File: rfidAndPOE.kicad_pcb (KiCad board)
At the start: 4 copper layers, 100 x 50 mm, 126 parts, among them J1 0813-1X1T-57-F, J2 SWD, J3 MCU Port B, J4 MCU Port C, P1 PoE-, P2 PoE+, P3 GND, P4 +5V, P5 +12V, P6 +3V3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

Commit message: Placed and routed all isolated PoE components.
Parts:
- moved R9 146.9 mm to (123.1, 47.5)
- moved R1 141.5 mm to (120.1, 43.9)
- moved R8 141.1 mm to (120.1, 42.1)
- moved D4 122.6 mm to (127.4, 44.6), turned to 90 degrees
- moved D7 121.4 mm to (123.2, 45.7)
- moved Q3 8.56 mm to (123.5, 43.0), turned to 270 degrees
- moved D3 6.78 mm to (122.4, 39.5), turned to 90 degrees
- moved R6 6.50 mm to (124.3, 39.6), turned to 90 degrees
- moved U5 3.60 mm to (129.9, 61.5)
- moved U3 2.53 mm to (133.8, 46.9)
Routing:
- net /PVcc: track 14.7 -> 42.1 mm, vias 2 -> 3
- net Net-(R1-Pad1): track 0.00 -> 25.1 mm, vias 0 -> 2
- net Net-(D7-Pad1): track 0.00 -> 24.3 mm, vias 0 -> 3
- net GNDA: track 41.8 -> 61.2 mm, vias 8 -> 19
- net Net-(D7-Pad2): track 0.00 -> 8.62 mm
- net Net-(D4-Pad2): track 0.00 -> 6.55 mm
- net Net-(R6-Pad2): track 0.00 -> 2.70 mm
- net Net-(D3-Pad1): track 0.00 -> 2.04 mm
- added copper zone on B.Cu, net GNDA
- added copper zone on F.Cu, net GNDA

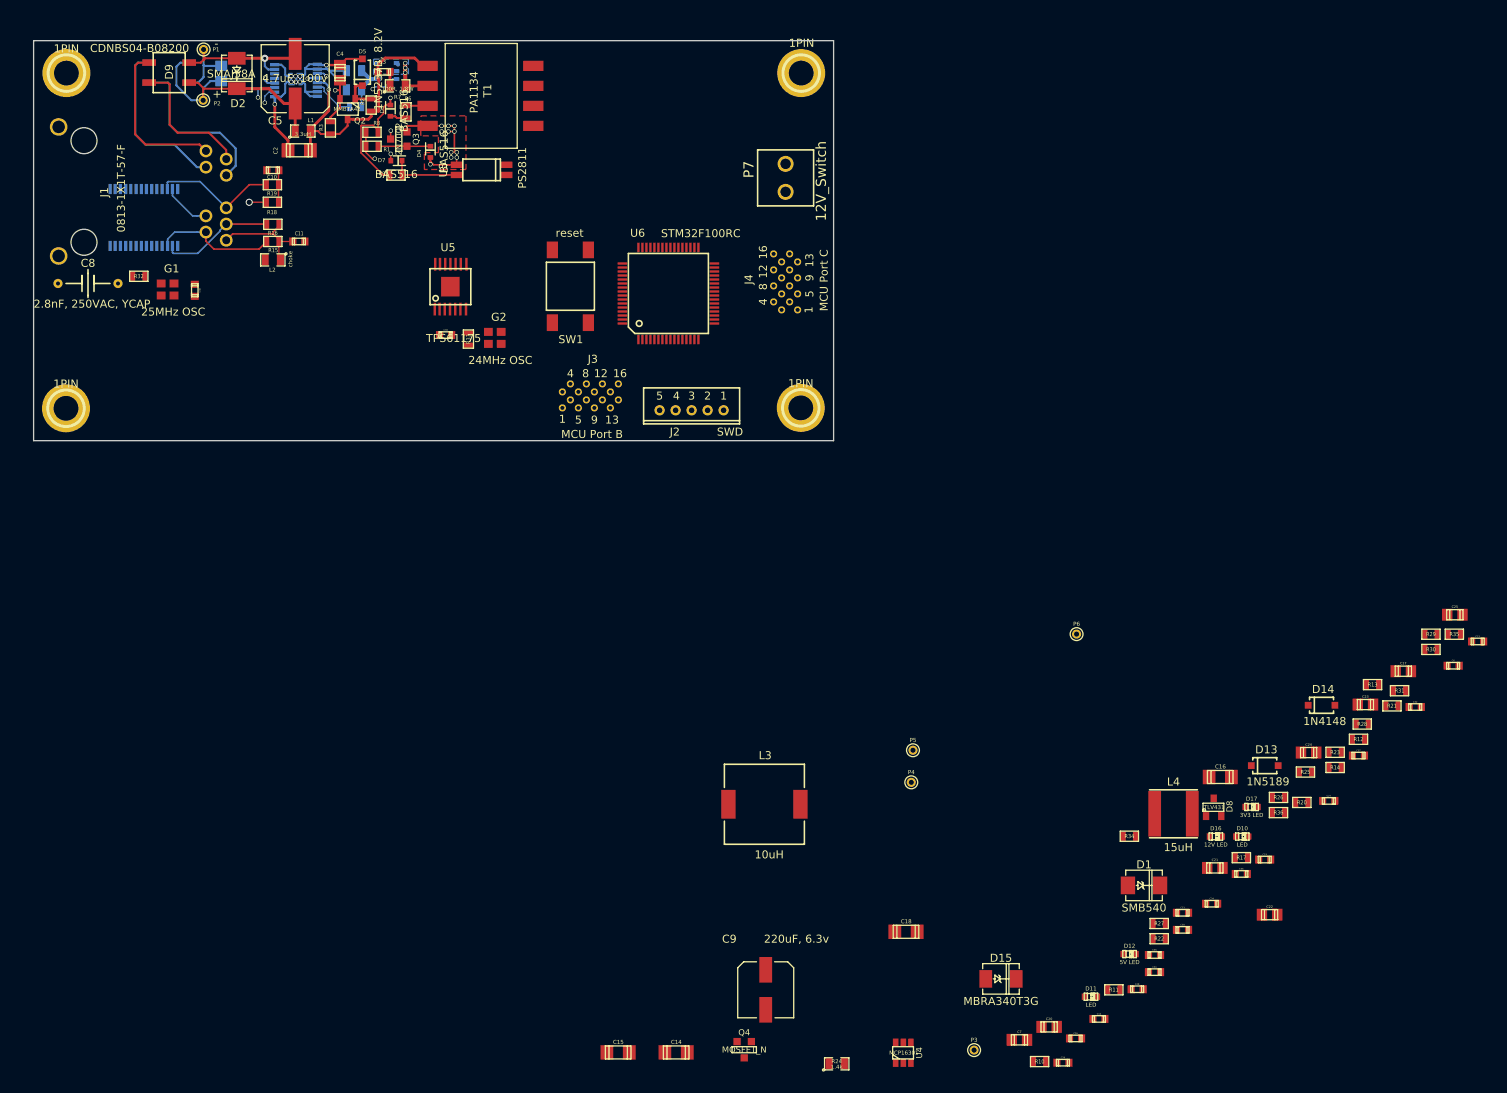
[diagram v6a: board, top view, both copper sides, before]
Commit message: Organized parts in to general sections (rest of PoE stuff, microcontroller, ethernet phy, 5v supply, and 3.3v supply are the groupings).
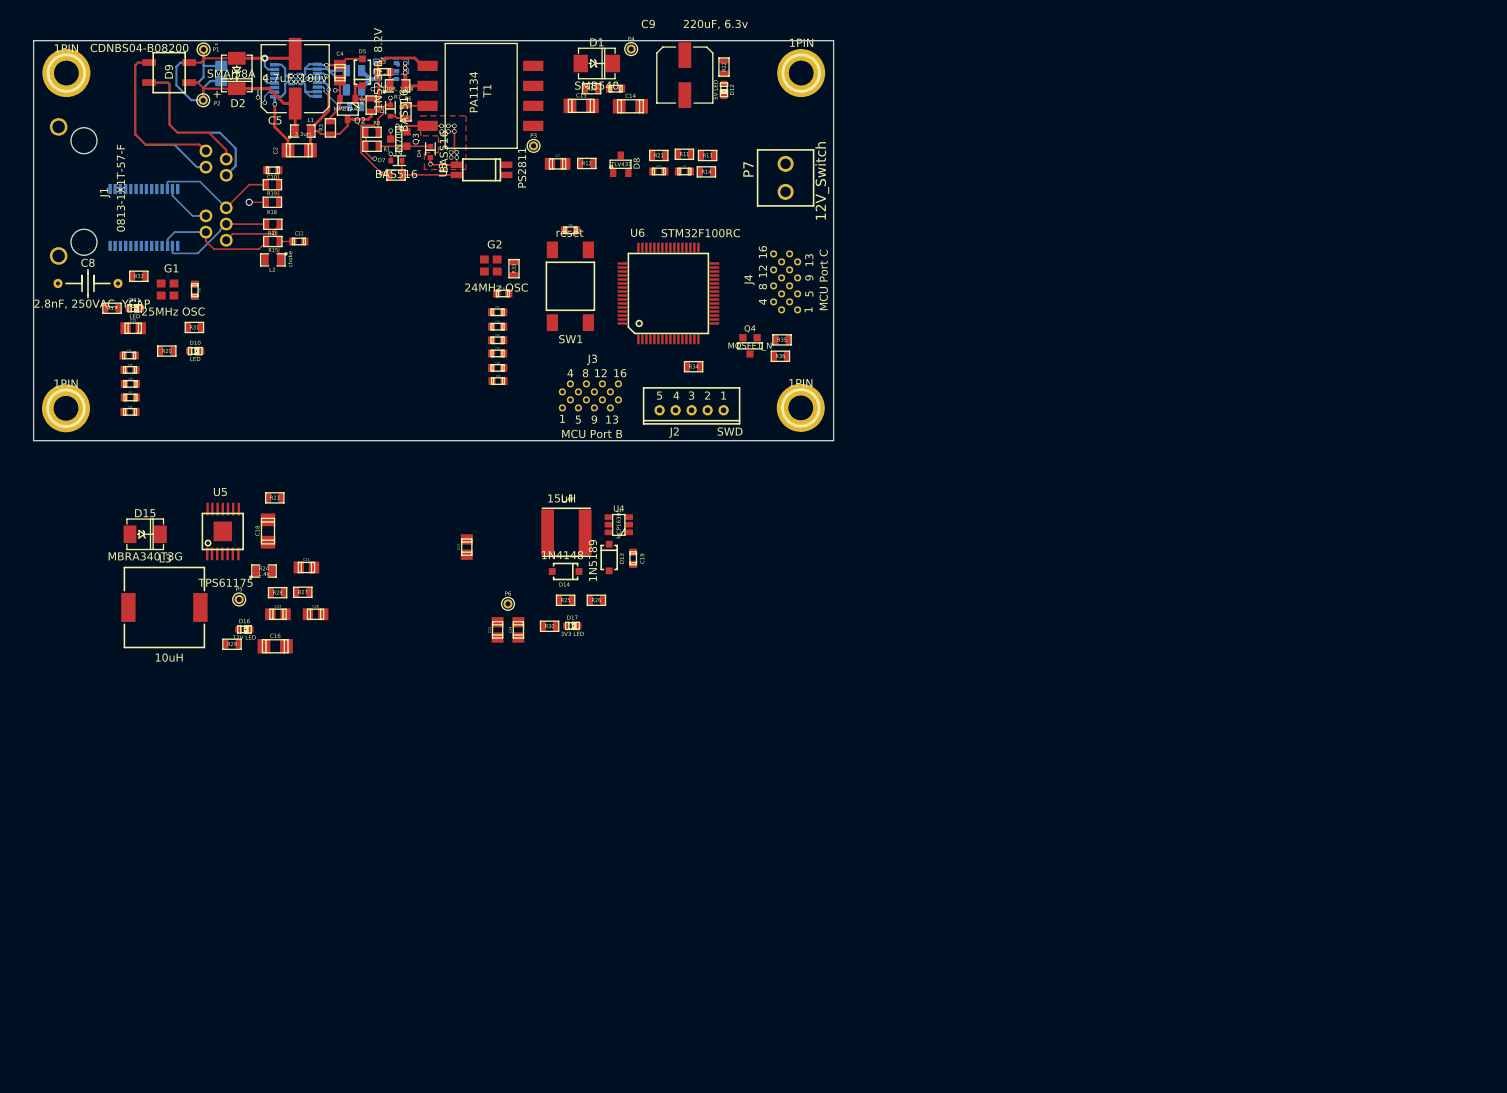
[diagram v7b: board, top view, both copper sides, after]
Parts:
- moved C25 169.0 mm to (90.2, 66.7)
- moved C27 158.1 mm to (89.9, 75.3)
- moved R31 157.3 mm to (97.9, 66.5)
- moved R17 157.0 mm to (87.6, 64.2)
- moved R20 152.7 mm to (94.5, 69.5)
- moved R29 149.9 mm to (102.6, 106.2)
- moved C31 149.6 mm to (89.8, 70.0)
- moved D11 147.3 mm to (90.5, 64.2)
- moved C28 146.8 mm to (89.9, 73.6)
- moved C29 145.3 mm to (89.8, 71.8)
- moved D10 144.3 mm to (98.0, 69.5)
- moved C26 141.8 mm to (89.8, 77.1)
- moved R28 136.6 mm to (108.3, 99.7)
- moved C23 136.4 mm to (108.3, 102.4)
- moved R23 136.3 mm to (108.0, 87.8)
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
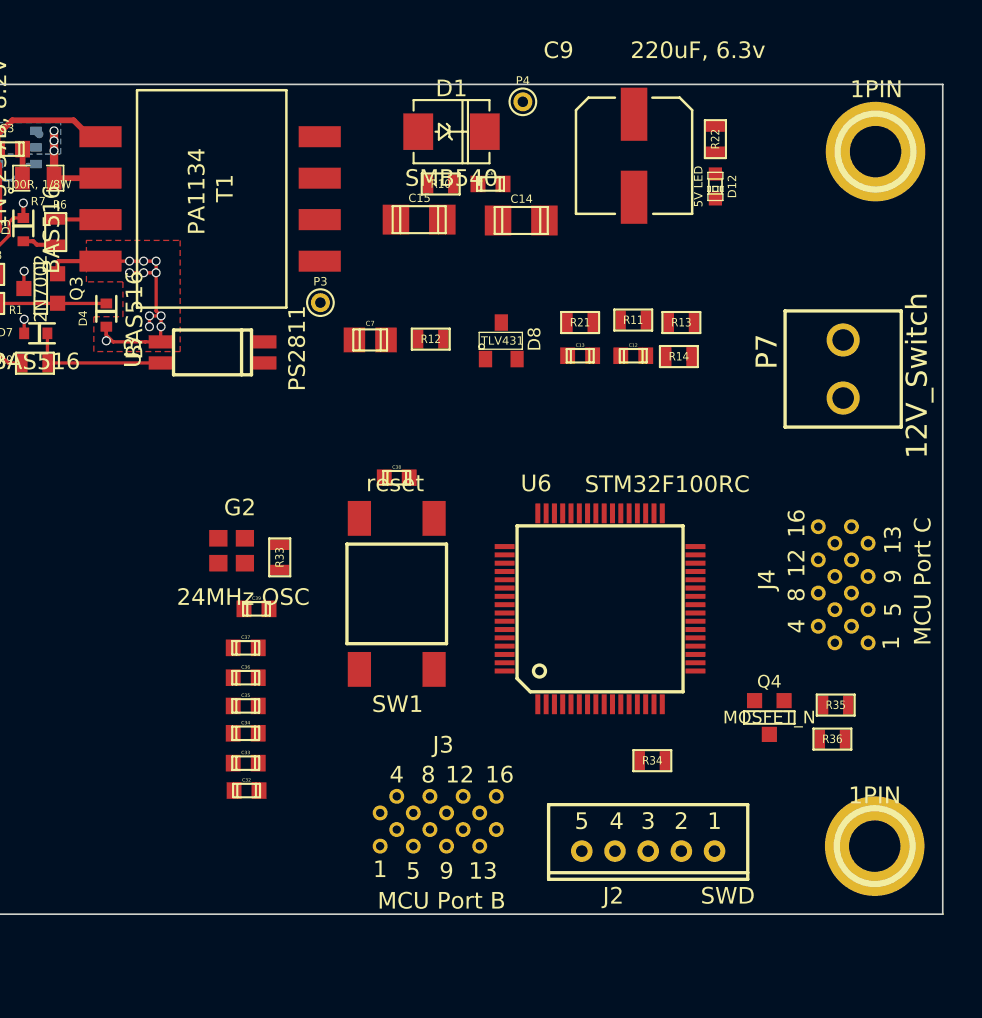
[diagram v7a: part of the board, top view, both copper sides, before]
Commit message: Fixed a schematic error where the gate resistor for the 12v switch was not connected to anything. Finished placing flyback feedback parts and almost routed all of them. Placed microcontroller parts just about where they will be going, but did not route anything.
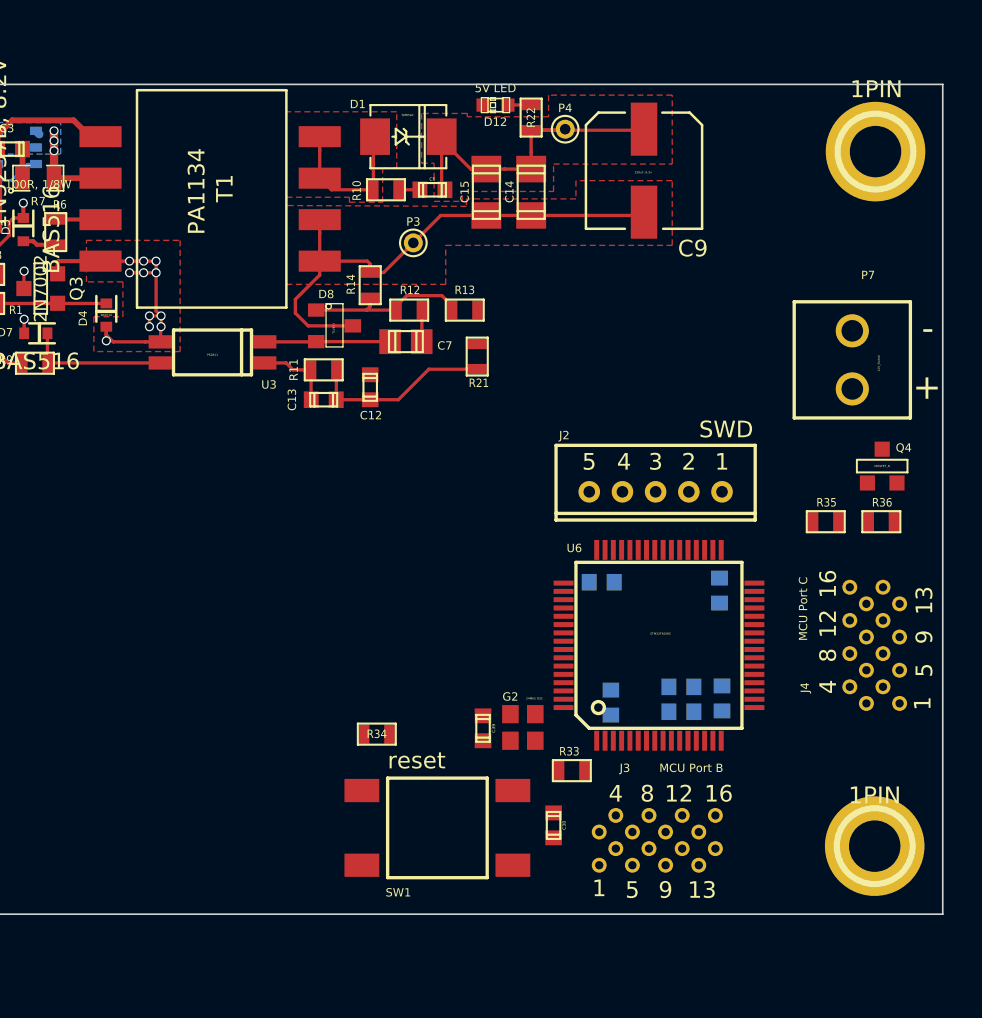
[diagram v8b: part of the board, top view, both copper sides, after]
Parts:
- C32, C33, C34, C35, C36, C37: moved to B.Cu
- moved C34 29.8 mm to (164.3, 61.2), turned to 90 degrees
- moved C35 28.7 mm to (164.5, 67.7), turned to 270 degrees
- moved C37 26.4 mm to (162.1, 67.0)
- moved C36 26.3 mm to (162.1, 68.5)
- moved C33 24.1 mm to (157.2, 60.7), turned to 180 degrees
- moved C38 23.0 mm to (154.3, 75.3), turned to 270 degrees
- moved C32 22.6 mm to (157.8, 68.0), turned to 270 degrees
- moved R33 21.8 mm to (155.4, 72.0), turned to 0 degrees
- moved J2 21.7 mm to (160.5, 55.2)
- moved G2 20.5 mm to (152.5, 69.5), turned to 270 degrees
- moved R14 19.1 mm to (143.3, 42.8), turned to 90 degrees
- moved R11 18.9 mm to (140.5, 47.9), turned to 180 degrees
- moved R34 16.7 mm to (143.7, 69.8)
- moved Q4 16.6 mm to (174.2, 53.7), turned to 180 degrees
- moved C12 16.0 mm to (143.3, 49.0), turned to 270 degrees
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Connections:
- R35 pad 2: Net-(R35-Pad2) -> /12VSwitch
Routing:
- net GND: track 0.00 -> 31.7 mm
- net 5VPoE: track 0.00 -> 20.8 mm
- net Net-(C12-Pad1): track 0.00 -> 11.1 mm
- net Net-(D8-Pad1): track 0.00 -> 10.0 mm
- net Net-(D1-Pad1): track 0.00 -> 9.26 mm
- net Net-(C7-Pad2): track 0.00 -> 7.58 mm
- net Net-(C13-Pad2): track 0.00 -> 4.79 mm
- net Net-(C7-Pad1): track 0.00 -> 1.90 mm
- net Net-(D12-Pad1): track 0.00 -> 1.41 mm
- net Net-(C6-Pad2): track 0.00 -> 1.29 mm
- added copper zone on F.Cu, net 5VPoE
- added copper zone on F.Cu, net GND
- added copper zone on F.Cu, net Net-(D1-Pad1)
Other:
- board text added: "+"
- board text added: "-"
